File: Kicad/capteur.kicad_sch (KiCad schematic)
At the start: 23 parts, among them J1 Power, J2 Digital/PWM, J3 Analog, J4 Digital/PWM, U2 LTC1050ACN8, U3 MCP41100

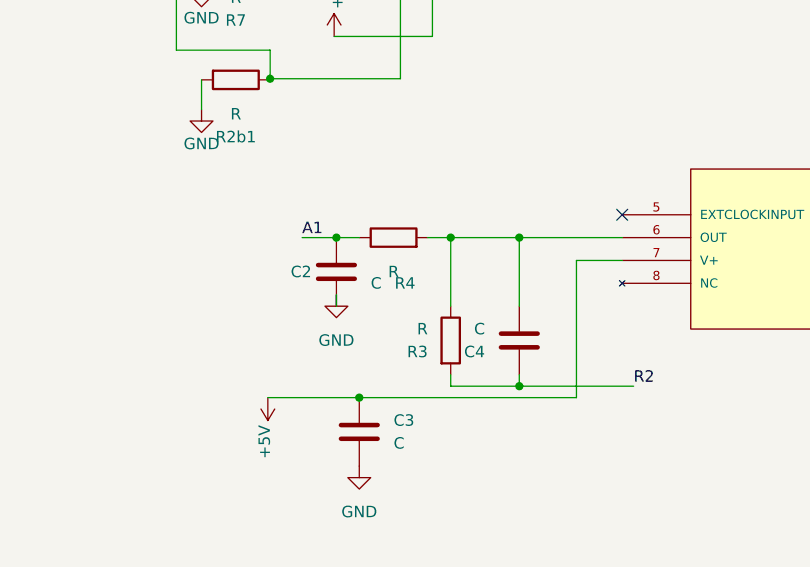
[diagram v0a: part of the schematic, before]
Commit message: Add of comments and calculation of graphite sensor resistance
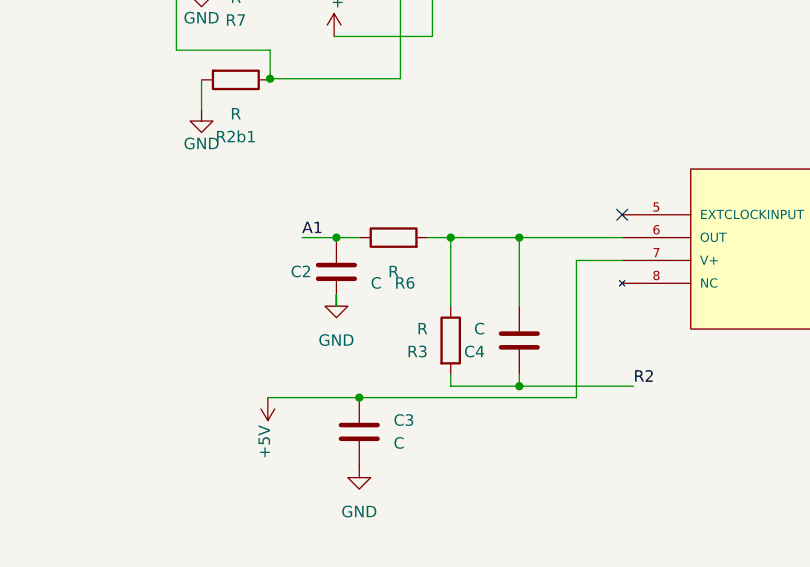
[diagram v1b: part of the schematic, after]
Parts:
- renumbered R4 to R6
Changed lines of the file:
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@@
   (symbol (lib_id "Device:R") (at 121.92 142.24 90) (unit 1)
     (in_bom yes) (on_board yes) (dnp no)
-    (property "Reference" "R4" (at 123.19 147.32 90)
+    (property "Reference" "R6" (at 123.19 147.32 90)
       (effects (font (size 1.27 1.27)))
     )
@@
       (project "capteur"
         (path "/e63e39d7-6ac0-4ffd-8aa3-1841a4541b55"
-          (reference "R4") (unit 1)
+          (reference "R6") (unit 1)
         )
       )

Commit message: minor change of kicad schematic
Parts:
- renumbered R6 to R9
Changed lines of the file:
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@@
   (symbol (lib_id "Device:R") (at 22.86 64.77 0) (unit 1)
     (in_bom yes) (on_board yes) (dnp no) (fields_autoplaced)
-    (property "Reference" "R6" (at 20.32 66.04 0)
-      (effects (font (size 1.27 1.27)) (justify right))
+    (property "Reference" "R9" (at 25.4 63.5 0)
+      (effects (font (size 1.27 1.27)) (justify left))
     )
-    (property "Value" "R" (at 20.32 63.5 0)
-      (effects (font (size 1.27 1.27)) (justify right))
+    (property "Value" "R" (at 25.4 66.04 0)
+      (effects (font (size 1.27 1.27)) (justify left))
     )
     (property "Footprint" "Library_Empreinte:R_Axial_DIN0207_L6.3mm_D2.5mm_P5.08mm_Vertical" (at 21.082 64.77 90)
@@
       (project "capteur"
         (path "/e63e39d7-6ac0-4ffd-8aa3-1841a4541b55"
-          (reference "R6") (unit 1)
+          (reference "R9") (unit 1)
         )
       )
